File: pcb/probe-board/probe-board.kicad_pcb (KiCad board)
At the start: 4 copper layers, 72.4 x 64 mm, 51 parts, among them J1 Conn_ARM_SWD_TagConnect_TC203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, J2 USB_C_Receptacle_USB2.0_16P, U1 STM32G431KBUx, U12 LPS22HH, U13 LPS22HH, U2 SRV05-4, U3 AMS1117-3.3, U4 LPS22HH, U5 LPS22HH, U6 LPS22HH, U7 LPS22HH, U8 LPS22HH, U9 LPS22HH, Y1 16MHz

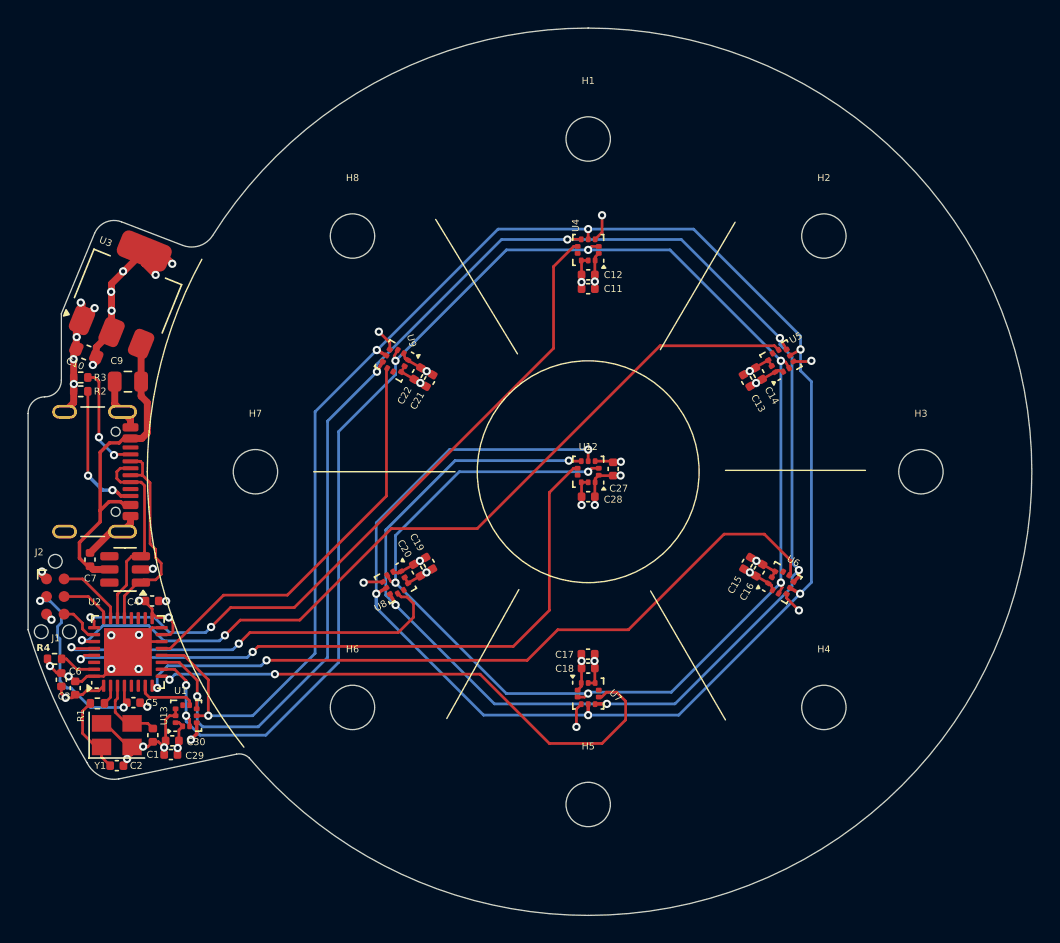
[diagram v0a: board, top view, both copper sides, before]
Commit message: Add feducials
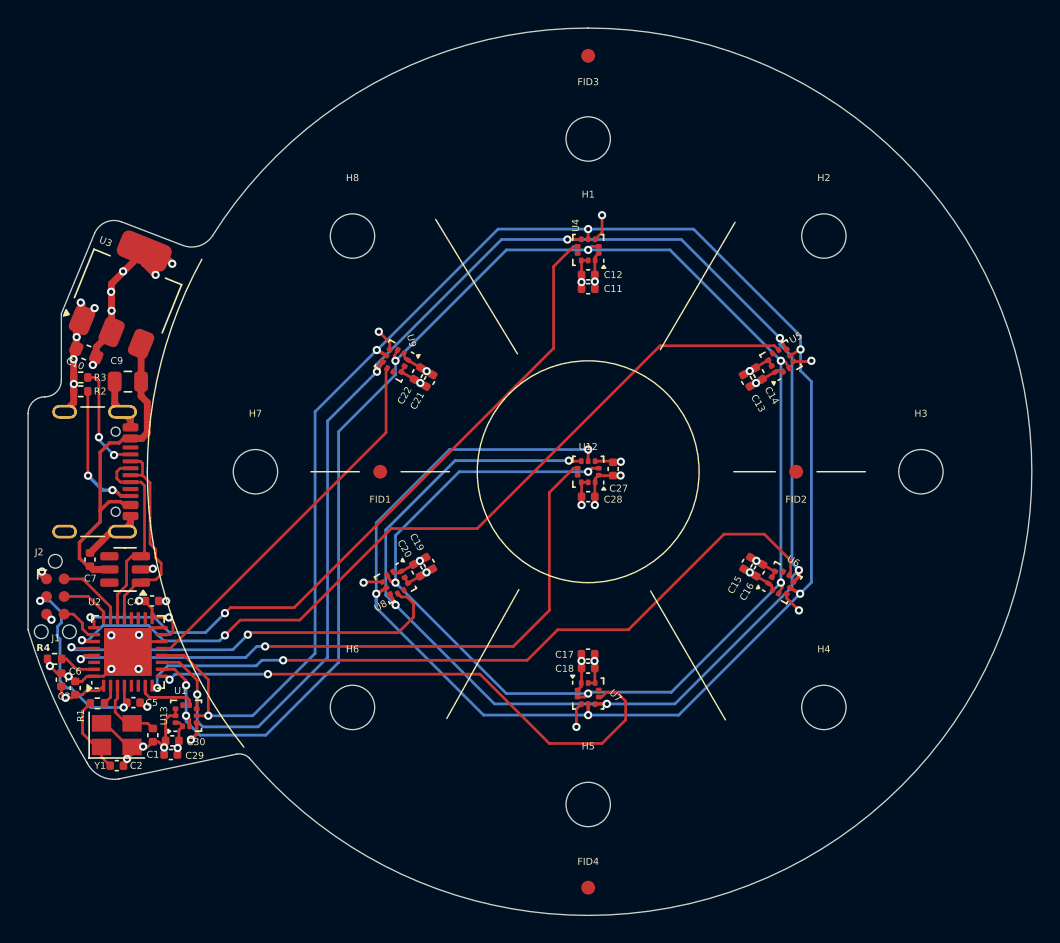
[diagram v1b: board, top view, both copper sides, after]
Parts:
- added FID1: Fiducial, Fiducial:Fiducial_1mm_Mask2mm, F.Cu at (145.0, 100.0)
- added FID2: Fiducial, Fiducial:Fiducial_1mm_Mask2mm, F.Cu at (175.0, 100.0)
- added FID3: Fiducial, Fiducial:Fiducial_1mm_Mask2mm, F.Cu at (160.0, 70.0)
- added FID4: Fiducial, Fiducial:Fiducial_1mm_Mask2mm, F.Cu at (160.0, 130.0)
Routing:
- net /CS6: track 30.0 -> 27.3 mm
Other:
- board text added: "Probe Board V1.1"
- board text removed: "Probe Board V1"

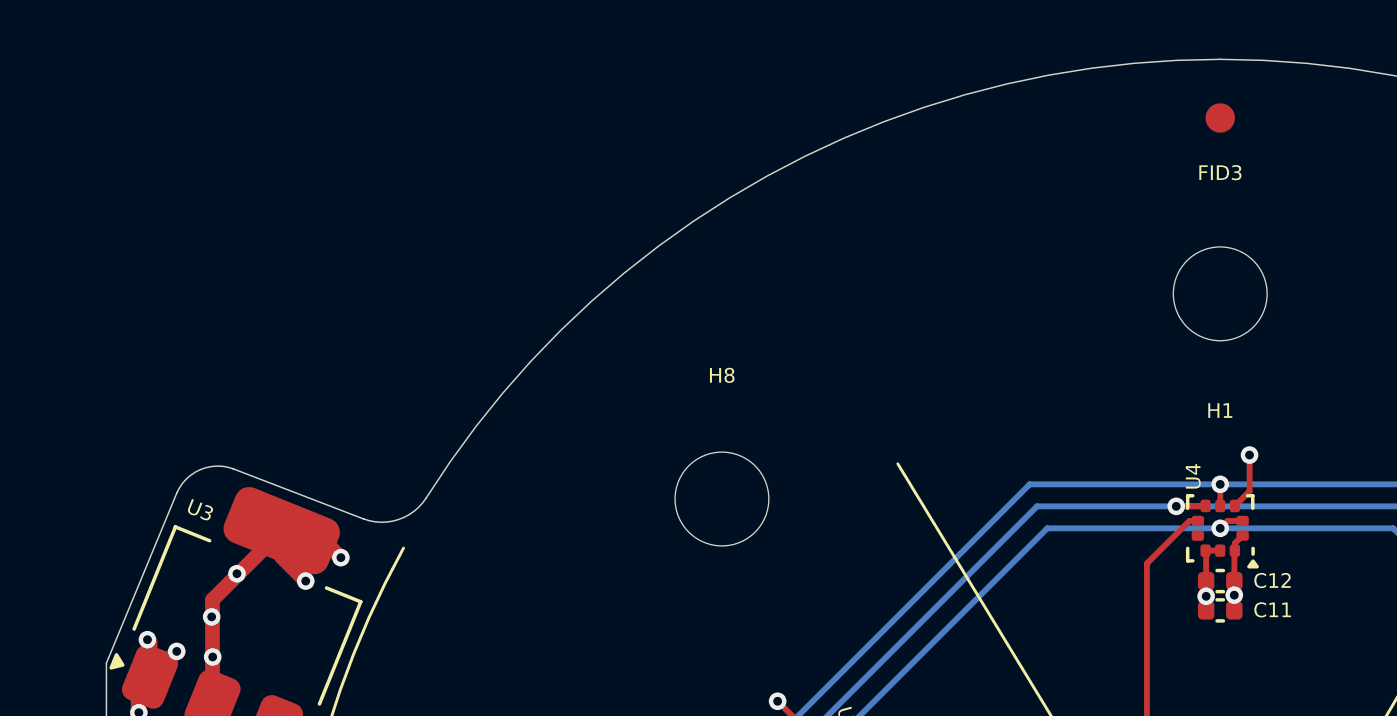
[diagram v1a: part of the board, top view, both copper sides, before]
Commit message: Add feducials and new manufacture data
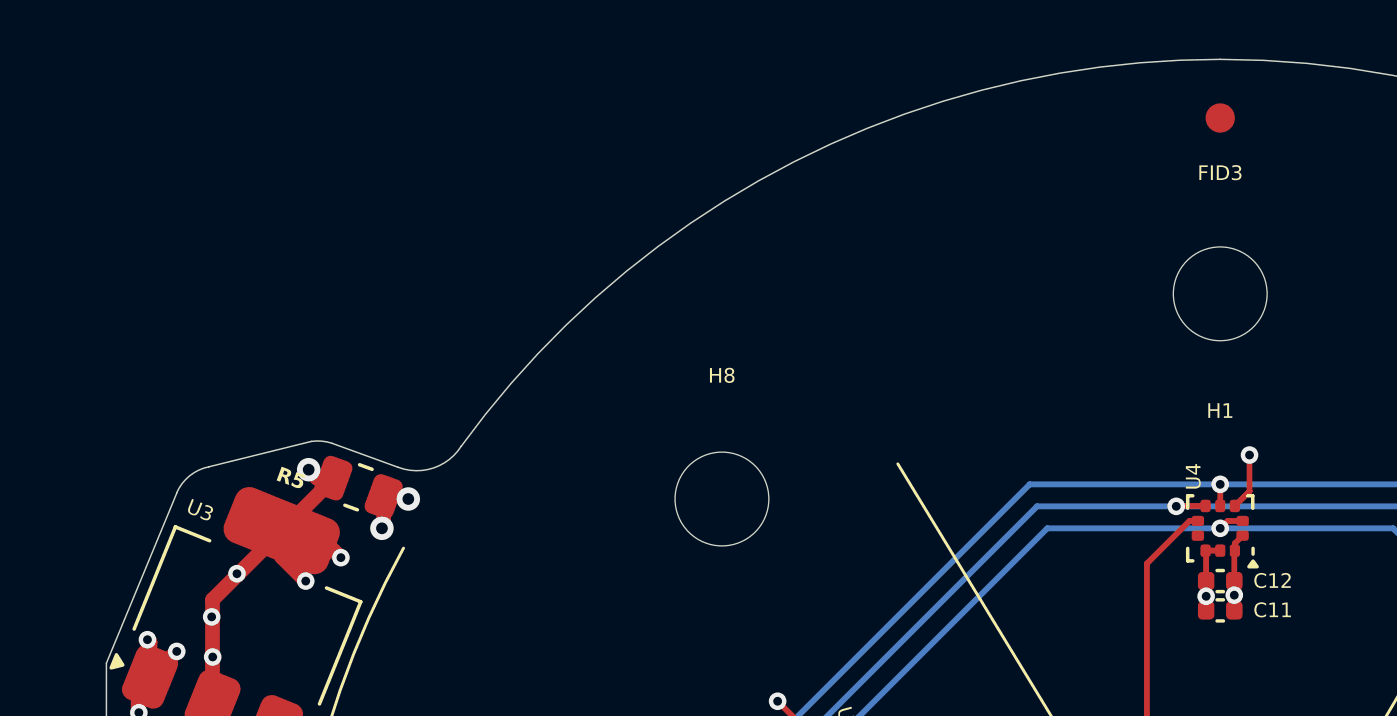
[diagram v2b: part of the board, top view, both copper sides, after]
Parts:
- added R5: 100, Resistor_SMD:R_0805_2012Metric, F.Cu at (130.6, 82.6)
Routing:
- net +3V3: track 47.4 -> 50.9 mm, vias 19 -> 20
- net GND: track 78.9 -> 80.9 mm, vias 33 -> 35
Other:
- outline, holes or cut-outs redrawn
